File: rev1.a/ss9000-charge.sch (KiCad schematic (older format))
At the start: 10 parts, among them U1 MCP73831, X1 USBMICRO

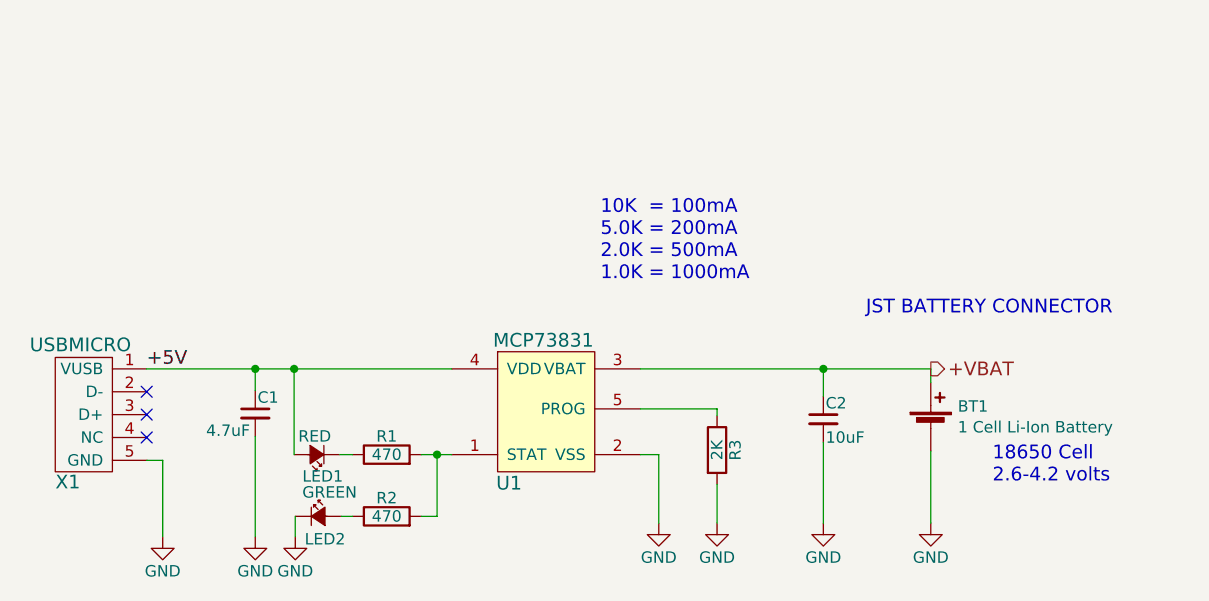
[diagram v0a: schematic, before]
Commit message: cosmetic changes to silk screen and updated schematic pdf
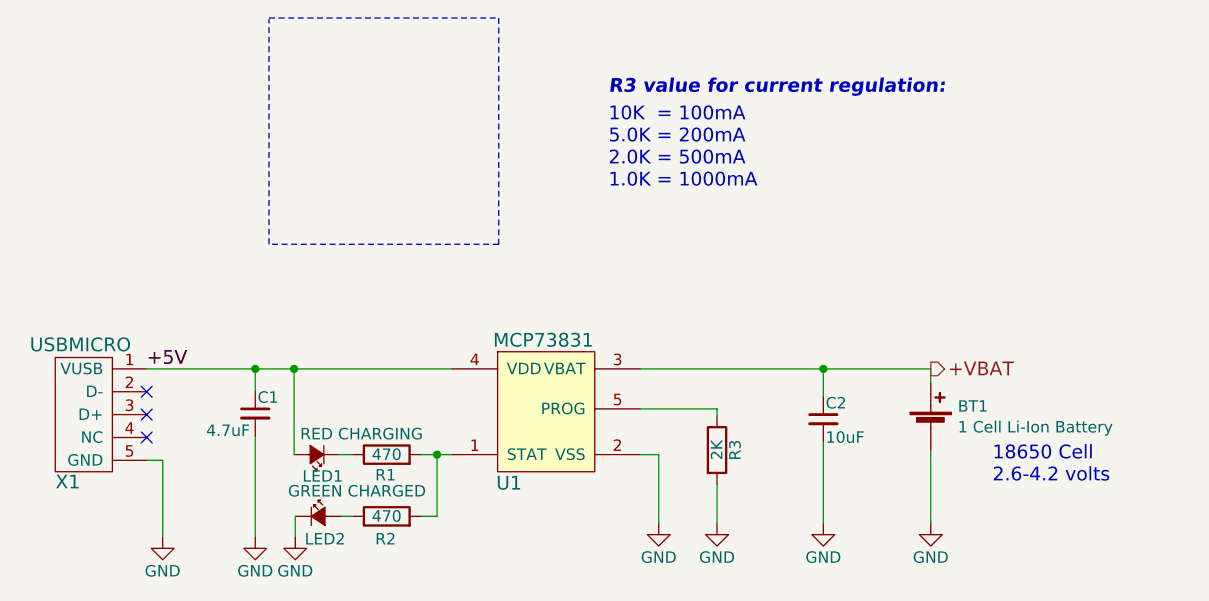
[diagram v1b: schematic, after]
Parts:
- LED1: value RED -> RED CHARGING
- LED2: value GREEN -> GREEN CHARGED
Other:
- note added: "R3 value for current regulation:"
- note removed: "JST BATTERY CONNECTOR"
